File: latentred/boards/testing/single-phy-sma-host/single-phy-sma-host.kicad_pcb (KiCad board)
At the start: 4 copper layers, 9 parts, among them J1 SMA, J2 SMA, J3 SMA, J4 SMA, J5 SMA, J6 SMA, J7 CONN_01X02, J8 CONN_01X08, J9 QSH-030-01-L-D-A

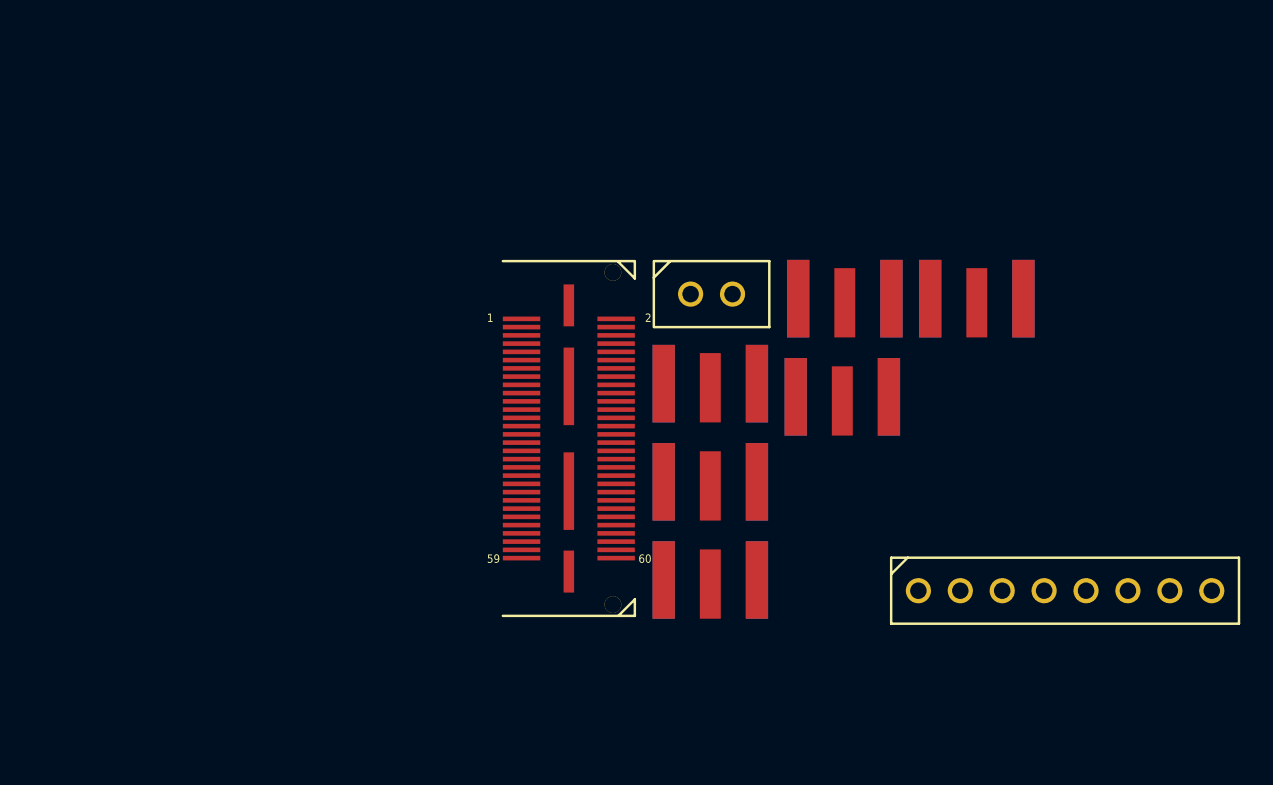
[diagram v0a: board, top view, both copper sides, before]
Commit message: Updated single-phy-sma-host with stitching vias and final layout
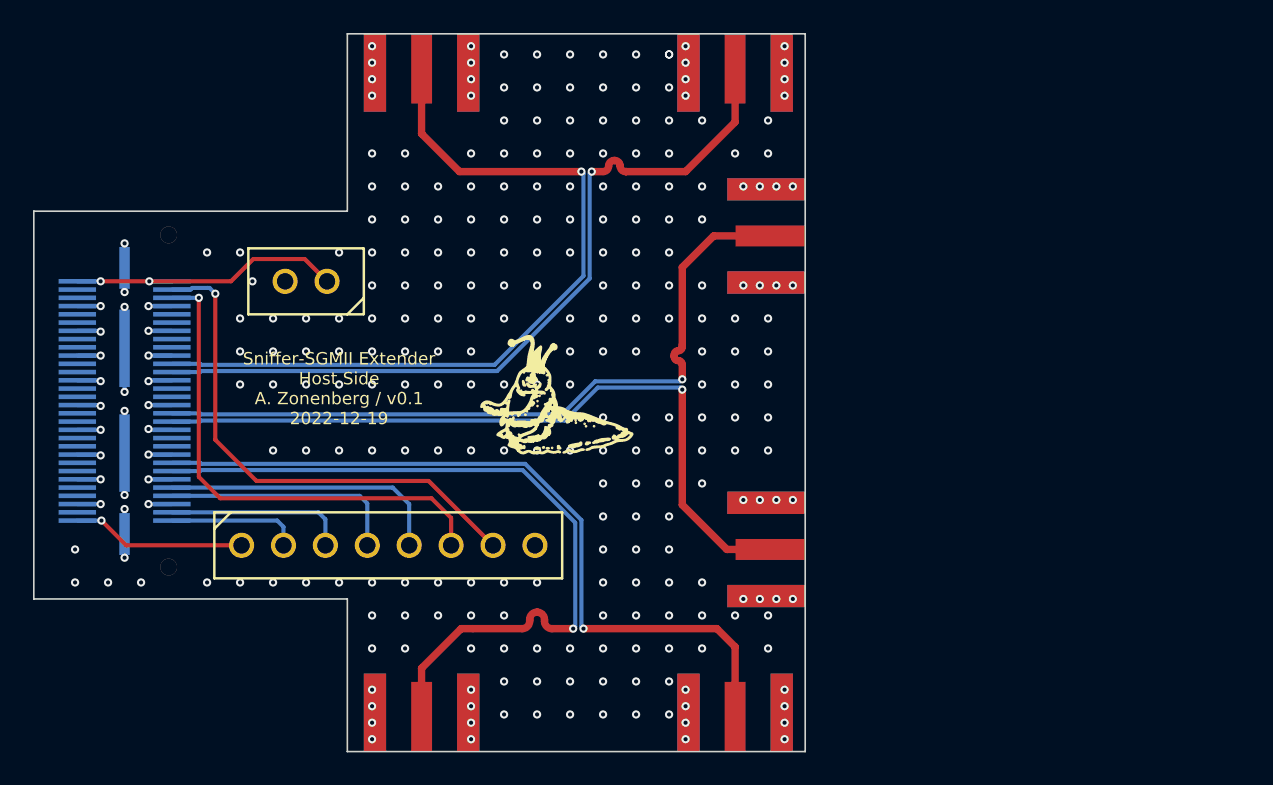
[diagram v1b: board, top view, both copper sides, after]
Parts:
- added G***: LOGO, azonenberg_pcb:LONGTHING-1200DPI, F.Cu at (97.8, 59.0)
- J9: moved to B.Cu
- moved J8 41.1 mm to (87.0, 67.8)
- moved J1 34.3 mm to (89.0, 36.8), turned to 180 degrees
- moved J9 27.0 mm to (71.0, 59.0)
- moved J5 25.9 mm to (108.0, 80.2)
- moved J7 24.6 mm to (82.0, 51.8), turned to 180 degrees
- moved J2 23.5 mm to (108.0, 36.8), turned to 180 degrees
- moved J6 19.3 mm to (89.0, 80.2)
- moved J3 12.3 mm to (112.2, 49.0), turned to 90 degrees
- moved J4 9.60 mm to (112.2, 68.0), turned to 90 degrees
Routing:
- net /GND: track 0.00 -> 691.6 mm, vias 0 -> 281
- net /SGMII_TX_P: track 0.00 -> 48.1 mm, vias 0 -> 1
- net /SGMII_TX_N: track 0.00 -> 48.1 mm, vias 0 -> 1
- net /SGMII_RX_P: track 0.00 -> 46.8 mm, vias 0 -> 1
- net /SGMII_RX_N: track 0.00 -> 46.5 mm, vias 0 -> 1
- net /SGMII_CLKOUT_N: track 0.00 -> 45.3 mm, vias 0 -> 1
- net /SGMII_CLKOUT_P: track 0.00 -> 45.3 mm, vias 0 -> 1
- net /MGMT_MDC: track 0.00 -> 31.2 mm, vias 0 -> 1
- net /MGMT_MDIO: track 0.00 -> 30.5 mm, vias 0 -> 1
- net /5V0: track 0.00 -> 17.6 mm, vias 0 -> 2
- net /PHY_RST_N: track 0.00 -> 17.3 mm
- net /GPIO_0: track 0.00 -> 14.6 mm
- net /GPIO_1: track 0.00 -> 11.1 mm
- net /PHY_INT_N: track 0.00 -> 10.6 mm, vias 0 -> 1
- net /PGOOD: track 0.00 -> 8.04 mm
- added copper zone on In1.Cu, net /GND
- added copper zone on In2.Cu, net /GND
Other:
- board outline added: 46.8 x 43.5 mm
- board text added: "Sniffer-SGMII Extender Host Side A. Zonenberg / v0.1 2022-12-19"

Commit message: Updated single-phy design with mask cutout and silkscreen fixes
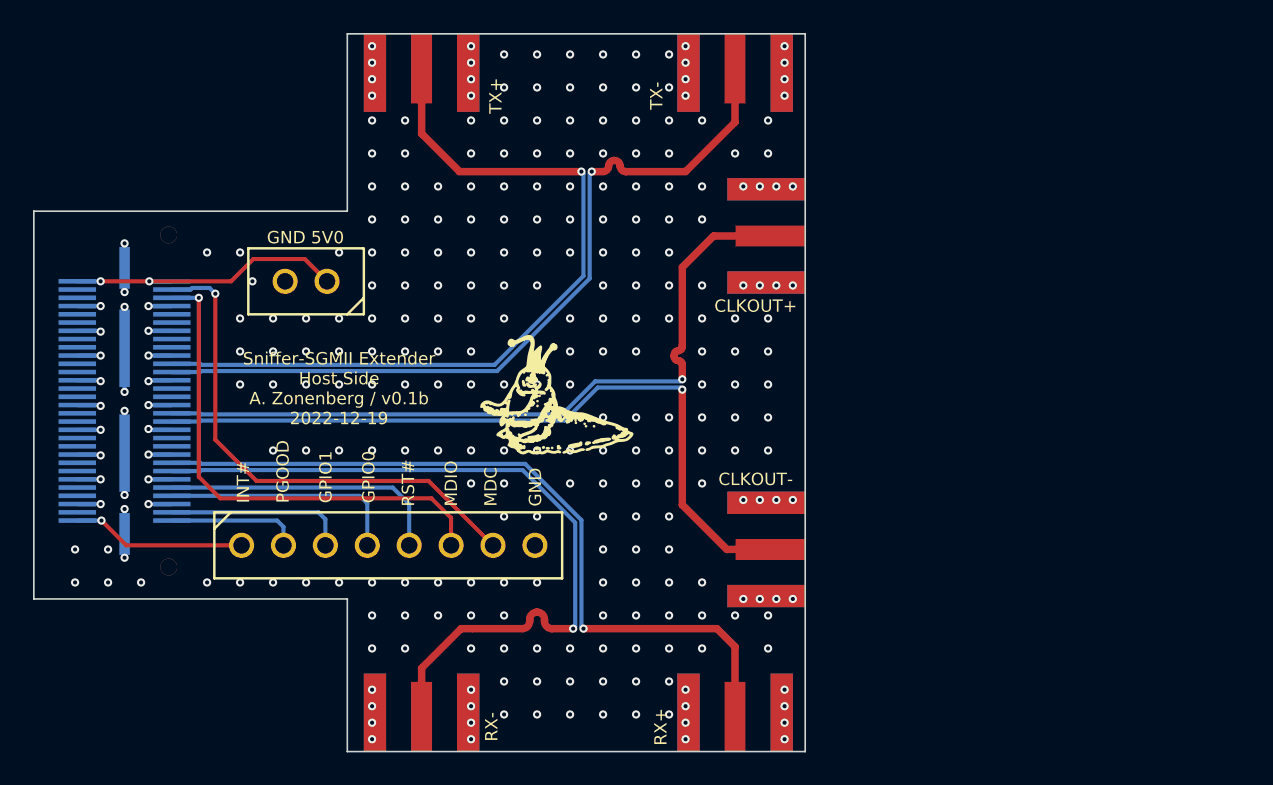
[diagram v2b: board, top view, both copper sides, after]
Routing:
- net /GND: track 691.6 -> 711.6 mm, vias 281 -> 289
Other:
- board text added: "5V0"
- board text added: "CLKOUT+"
- board text added: "CLKOUT-"
- board text added: "GND"
- board text added: "GPIO0"
- board text added: "GPIO1"
- board text added: "INT#"
- board text added: "MDC"
- board text added: "MDIO"
- board text added: "PGOOD"
- board text added: "RST#"
- board text added: "RX+"
- board text added: "RX-"
- board text added: "Sniffer-SGMII Extender Host Side A. Zonenberg / v0.1b 2022-12-19"
- board text added: "TX+"
- board text added: "TX-"
- board text removed: "Sniffer-SGMII Extender Host Side A. Zonenberg / v0.1 2022-12-19"
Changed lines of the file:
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@@
   (gr_line (start 65.5 47.5) (end 84.5 47.5) (layer "Edge.Cuts") (width 0.1))
   (gr_line (start 84.5 36.75) (end 112.25 36.75) (layer "Edge.Cuts") (width 0.1))
-  (gr_text "Sniffer-SGMII Extender\nHost Side\nA. Zonenberg / v0.1\n2022-12-19" (at 84 58.25) (layer "F.SilkS")
-    (effects (font (size 0.75 0.75) (thickness 0.1)))
+  (gr_text "RST#" (at 88.2 65.4 90) (layer "F.SilkS")
+    (effects (font (size 0.75 0.75) (thickness 0.1)) (justify left))
+  )
+  (gr_text "RX+" (at 103.5 78.75 90) (layer "F.SilkS")
+    (effects (font (size 0.75 0.75) (thickness 0.1)))
+  )
+  (gr_text "GPIO0" (at 85.8 65.2 90) (layer "F.SilkS")
+    (effects (font (size 0.75 0.75) (thickness 0.1)) (justify left))
+  )
+  (gr_text "RX-" (at 93.25 78.75 90) (layer "F.SilkS")
+    (effects (font (size 0.75 0.75) (thickness 0.1)))
+  )
+  (gr_text "TX+" (at 93.5 40.5 90) (layer "F.SilkS")
+    (effects (font (size 0.75 0.75) (thickness 0.1)))
+  )
+  (gr_text "CLKOUT+" (at 109.25 53.25) (layer "F.SilkS")
+    (effects (font (size 0.75 0.75) (thickness 0.1)))
+  )
+  (gr_text "GND" (at 95.9 65.4 90) (layer "F.SilkS")
+    (effects (font (size 0.75 0.75) (thickness 0.1)) (justify left))
+  )
+  (gr_text "GPIO1" (at 83.2 65.2 90) (layer "F.SilkS")
+    (effects (font (size 0.75 0.75) (thickness 0.1)) (justify left))
+  )
+  (gr_text "INT#" (at 78.2 65.2 90) (layer "F.SilkS")
+    (effects (font (size 0.75 0.75) (thickness 0.1)) (justify left))
+  )
+  (gr_text "MDIO" (at 90.8 65.4 90) (layer "F.SilkS")
+    (effects (font (size 0.75 0.75) (thickness 0.1)) (justify left))
+  )
+  (gr_text "5V0" (at 83.3 49.1) (layer "F.SilkS")
+    (effects (font (size 0.75 0.75) (thickness 0.1)))
+  )
+  (gr_text "PGOOD" (at 80.6 65.2 90) (layer "F.SilkS")
+    (effects (font (size 0.75 0.75) (thickness 0.1)) (justify left))
+  )
+  (gr_text "CLKOUT-" (at 109.25 63.75) (layer "F.SilkS")
+    (effects (font (size 0.75 0.75) (thickness 0.1)))
+  )
+  (gr_text "GND" (at 80.8 49.1) (layer "F.SilkS")
+    (effects (font (size 0.75 0.75) (thickness 0.1)))
+  )
+  (gr_text "Sniffer-SGMII Extender\nHost Side\nA. Zonenberg / v0.1b\n2022-12-19" (at 84 58.25) (layer "F.SilkS")
+    (effects (font (size 0.75 0.75) (thickness 0.1)))
+  )
+  (gr_text "TX-" (at 103.25 40.5 90) (layer "F.SilkS")
+    (effects (font (size 0.75 0.75) (thickness 0.1)))
+  )
+  (gr_text "MDC" (at 93.2 65.4 90) (layer "F.SilkS")
+    (effects (font (size 0.75 0.75) (thickness 0.1)) (justify left))
   )
   (segment (start 89 38.875) (end 89 42.8) (width 0.45) (layer "F.Cu") (net 1))
@@
   (via (at 86 70) (size 0.5) (drill 0.25) (layers "F.Cu" "B.Cu") (net 2))
   (via (at 84 54) (size 0.5) (drill 0.25) (layers "F.Cu" "B.Cu") (net 2))
+  (via (at 70 68) (size 0.5) (drill 0.25) (layers "F.Cu" "B.Cu") (net 2))
+  (via (at 96 66) (size 0.5) (drill 0.25) (layers "F.Cu" "B.Cu") (net 2))
   (via (at 84 62) (size 0.5) (drill 0.25) (layers "F.Cu" "B.Cu") (net 2))
   (via (at 86 78.5) (size 0.5) (drill 0.25) (layers "F.Cu" "B.Cu") (net 2))
   (via (at 110 60) (size 0.5) (drill 0.25) (layers "F.Cu" "B.Cu") (net 2))
+  (via (at 92 42) (size 0.5) (drill 0.25) (layers "F.Cu" "B.Cu") (net 2))
+  (via (at 86 42) (size 0.5) (drill 0.25) (layers "F.Cu" "B.Cu") (net 2))
   (via (at 110 56) (size 0.5) (drill 0.25) (layers "F.Cu" "B.Cu") (net 2))
   (via (at 92 39.5) (size 0.5) (drill 0.25) (layers "F.Cu" "B.Cu") (net 2))
@@
   (via (at 86 56) (size 0.5) (drill 0.25) (layers "F.Cu" "B.Cu") (net 2))
   (via (at 86 74) (size 0.5) (drill 0.25) (layers "F.Cu" "B.Cu") (net 2))
+  (via (at 94 66) (size 0.5) (drill 0.25) (layers "F.Cu" "B.Cu") (net 2))
   (via (at 105 37.5) (size 0.5) (drill 0.25) (layers "F.Cu" "B.Cu") (net 2))
   (via (at 105 79.5) (size 0.5) (drill 0.25) (layers "F.Cu" "B.Cu") (net 2))
@@
   (via (at 86 39.5) (size 0.5) (drill 0.25) (layers "F.Cu" "B.Cu") (net 2))
   (via (at 102 42) (size 0.5) (drill 0.25) (layers "F.Cu" "B.Cu") (net 2))
+  (via (at 92 64) (size 0.5) (drill 0.25) (layers "F.Cu" "B.Cu") (net 2))
   (via (at 68 68) (size 0.5) (drill 0.25) (layers "F.Cu" "B.Cu") (net 2))
   (via (at 100 46) (size 0.5) (drill 0.25) (layers "F.Cu" "B.Cu") (net 2))
   (via (at 102 46) (size 0.5) (drill 0.25) (layers "F.Cu" "B.Cu") (net 2))
+  (via (at 94 64) (size 0.5) (drill 0.25) (layers "F.Cu" "B.Cu") (net 2))
   (via (at 96 38) (size 0.5) (drill 0.25) (layers "F.Cu" "B.Cu") (net 2))
   (via (at 88 72) (size 0.5) (drill 0.25) (layers "F.Cu" "B.Cu") (net 2))
@@
   (via (at 92 46) (size 0.5) (drill 0.25) (layers "F.Cu" "B.Cu") (net 2))
   (via (at 71 49.45) (size 0.5) (drill 0.25) (layers "F.Cu" "B.Cu") (net 2))
+  (via (at 98 64) (size 0.5) (drill 0.25) (layers "F.Cu" "B.Cu") (net 2))
   (via (at 86 58) (size 0.5) (drill 0.25) (layers "F.Cu" "B.Cu") (net 2))
   (via (at 68 70) (size 0.5) (drill 0.25) (layers "F.Cu" "B.Cu") (net 2))
@@
   (via (at 94 44) (size 0.5) (drill 0.25) (layers "F.Cu" "B.Cu") (net 2))
   (via (at 80 54) (size 0.5) (drill 0.25) (layers "F.Cu" "B.Cu") (net 2))
+  (via (at 88 42) (size 0.5) (drill 0.25) (layers "F.Cu" "B.Cu") (net 2))
   (via (at 88 52) (size 0.5) (drill 0.25) (layers "F.Cu" "B.Cu") (net 2))
   (via (at 98 48) (size 0.5) (drill 0.25) (layers "F.Cu" "B.Cu") (net 2))
@@
   (via (at 86 44) (size 0.5) (drill 0.25) (layers "F.Cu" "B.Cu") (net 2))
   (via (at 72.45 54.75) (size 0.5) (drill 0.25) (layers "F.Cu" "B.Cu") (net 2))
-  (via (at 104 38) (size 0.5) (drill 0.25) (layers "F.Cu" "B.Cu") (net 2))
   (via (at 92 52) (size 0.5) (drill 0.25) (layers "F.Cu" "B.Cu") (net 2))
   (via (at 111.500001 71) (size 0.5) (drill 0.25) (layers "F.Cu" "B.Cu") (net 2))
@@
   (segment (start 91.5 42) (end 105 42) (width 0.125) (layer "In1.Cu") (net 2))
   (segment (start 106 70) (end 86 70) (width 0.125) (layer "In1.Cu") (net 2))
+  (segment (start 100 64) (end 92 64) (width 0.125) (layer "In1.Cu") (net 2))
   (segment (start 69.55 59.3) (end 69.55 57.8) (width 0.25) (layer "In1.Cu") (net 2))
   (segment (start 102 60) (end 102 70) (width 0.125) (layer "In1.Cu") (net 2))
@@
   (segment (start 94 78) (end 104 78) (width 0.125) (layer "In1.Cu") (net 2))
   (segment (start 69.55 60.75) (end 69.55 59.3) (width 0.25) (layer "In1.Cu") (net 2))
+  (segment (start 100 66) (end 94 66) (width 0.125) (layer "In1.Cu") (net 2))
   (segment (start 105.5 41.5) (end 110.5 41.5) (width 0.125) (layer "In1.Cu") (net 2))
   (segment (start 72.45 62.25) (end 72.45 60.7) (width 0.25) (layer "In1.Cu") (net 2))
@@
   (segment (start 105 40.5) (end 105 41) (width 0.125) (layer "In1.Cu") (net 2))
   (segment (start 72.45 65.25) (end 71.25 65.25) (width 0.25) (layer "In1.Cu") (net 2))
+  (segment (start 70 68) (end 70 70) (width 0.125) (layer "In1.Cu") (net 2))
   (segment (start 111 37.5) (end 111 40.5) (width 0.25) (layer "In1.Cu") (net 2))
   (segment (start 106 46) (end 106 51.5) (width 0.125) (layer "In1.Cu") (net 2))
@@
   (segment (start 80 62) (end 102 62) (width 0.125) (layer "In1.Cu") (net 2))
   (segment (start 86 40.5) (end 86 41.45) (width 0.125) (layer "In1.Cu") (net 2))
+  (segment (start 102 56) (end 102 60) (width 0.125) (layer "In1.Cu") (net 2))
   (segment (start 86 41.45) (end 86 41.5) (width 0.125) (layer "In1.Cu") (net 2))
   (segment (start 105 76.5) (end 105 75) (width 0.125) (layer "In1.Cu") (net 2))
@@
       )
     )
+  )
+  (zone (net 0) (net_name "") (layer "F.Mask") (hatch edge 0.508)
+    (connect_pads (clearance 0.125))
+    (min_thickness 0.125) (filled_areas_thickness no)
+    (fill yes (thermal_gap 0.508) (thermal_bridge_width 0.508))
+    (polygon
+      (pts
+        (xy 107.5 49.5)
+        (xy 107 49.5)
+        (xy 105.5 51)
+        (xy 105.5 65.5)
+        (xy 107.5 67.5)
+        (xy 107.5 68.5)
+        (xy 107 68.5)
+        (xy 104.5 66)
+        (xy 104.5 57.5)
+        (xy 104 57)
+        (xy 104 56)
+        (xy 104.5 55.5)
+        (xy 104.5 50.5)
+        (xy 106.5 48.5)
+        (xy 107.5 48.5)
+      )
+    )
+  )
+  (zone (net 0) (net_name "") (layer "F.Mask") (hatch edge 0.508)
+    (connect_pads (clearance 0.125))
+    (min_thickness 0.125) (filled_areas_thickness no)
+    (fill yes (thermal_gap 0.508) (thermal_bridge_width 0.508))
+    (polygon
+      (pts
+        (xy 89.5 42.5)
+        (xy 91.5 44.5)
+        (xy 99.5 44.5)
+        (xy 100 44)
+        (xy 101.5 44)
+        (xy 102 44.5)
+        (xy 105 44.5)
+        (xy 107.5 42)
+        (xy 107.5 41.5)
+        (xy 108.5 41.5)
+        (xy 108.5 42.5)
+        (xy 105.5 45.5)
+        (xy 91 45.5)
+        (xy 88.5 43)
+        (xy 88.5 41.5)
+        (xy 89.5 41.5)
+      )
+    )
+  )
+  (zone (net 0) (net_name "") (layer "F.Mask") (hatch edge 0.508)
+    (connect_pads (clearance 0.125))
+    (min_thickness 0.125) (filled_areas_thickness no)
+    (fill yes (thermal_gap 0.508) (thermal_bridge_width 0.508))
+    (polygon
+      (pts
+        (xy 97 72)
+        (xy 97 72.5)
+        (xy 107.5 72.5)
+        (xy 108.5 73.5)
+        (xy 108.5 75.5)
+        (xy 107.5 75.5)
+        (xy 107.5 74)
+        (xy 107 73.5)
+        (xy 91.5 73.5)
+        (xy 89.5 75.5)
+        (xy 88.5 75.5)
+        (xy 88.5 75)
+        (xy 91 72.5)
+        (xy 95 72.5)
+        (xy 95 72)
+        (xy 95.5 71.5)
+        (xy 96.5 71.5)
+      )
+    )
